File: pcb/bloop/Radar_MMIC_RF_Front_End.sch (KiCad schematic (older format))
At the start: 1 part

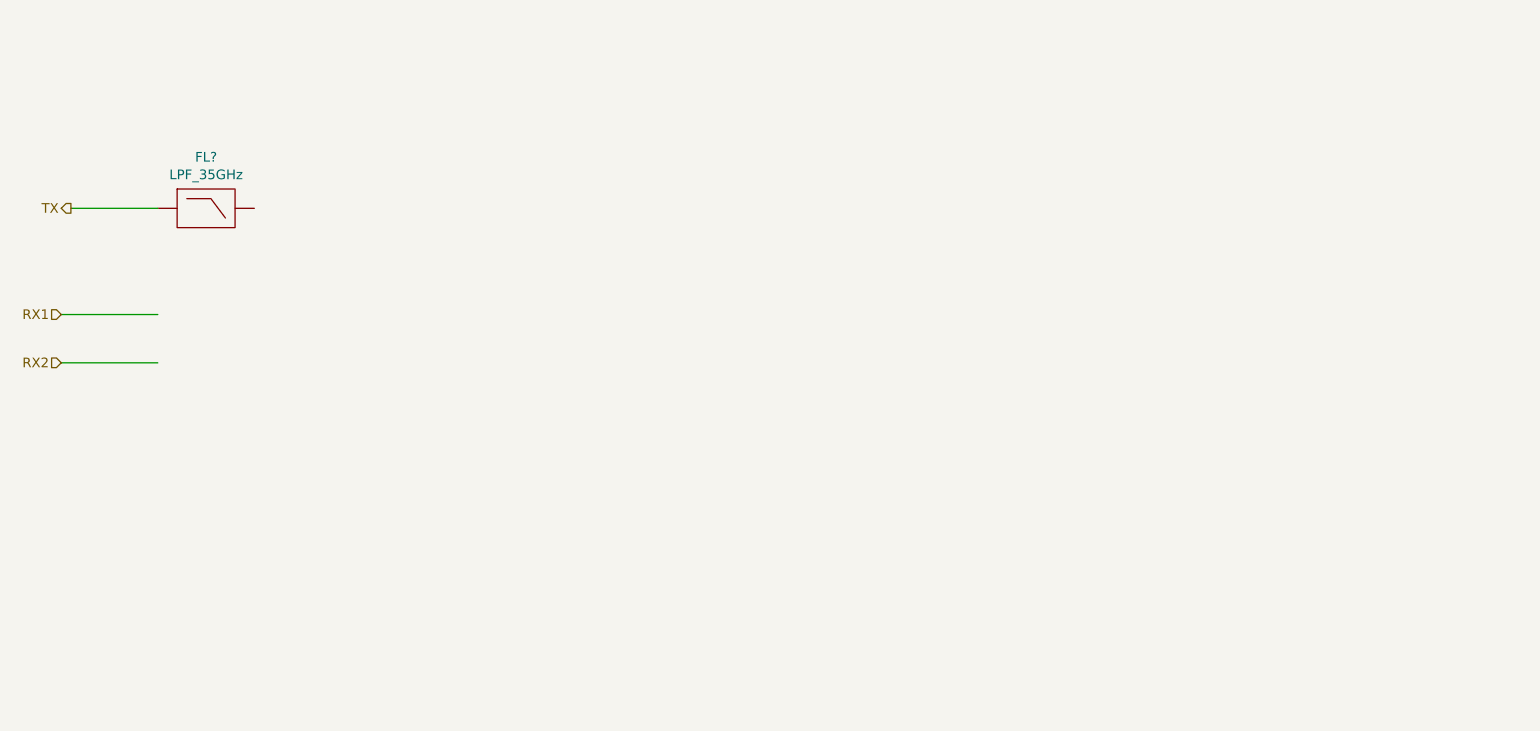
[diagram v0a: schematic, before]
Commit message: Added 3d SMP footprint and model
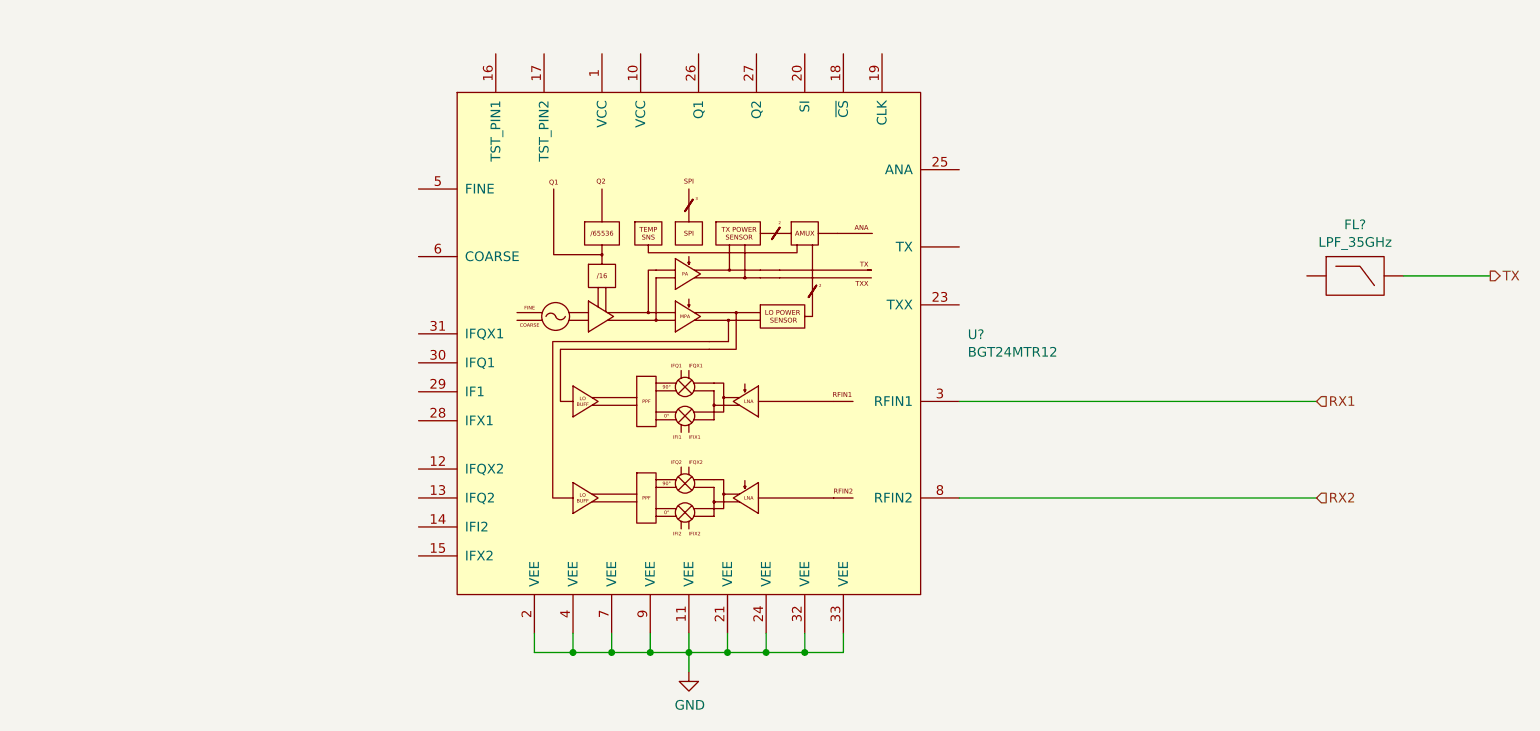
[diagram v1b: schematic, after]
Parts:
- added U?: BGT24MTR12, symbol bloop:BGT24MTR12
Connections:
- net labels added: GND
- wire segments 3 -> 21
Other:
- moved on the sheet: FL?
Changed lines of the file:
@@
 L bloop:LPF_35GHz FL?
 U 1 1 5D3D6E0E
-P 3200 2500
-F 0 "FL?" H 3200 2765 50  0000 C CNN
-F 1 "LPF_35GHz" H 3200 2674 50  0000 C CNN
-F 2 "bloop:35GHz_LPF" H 3200 2250 50  0001 C CNN
-F 3 "" H 2700 2750 50  0001 C CNN
-	1    3200 2500
+P 9150 2850
+F 0 "FL?" H 9150 3115 50  0000 C CNN
+F 1 "LPF_35GHz" H 9150 3024 50  0000 C CNN
+F 2 "bloop:35GHz_LPF" H 9150 2600 50  0001 C CNN
+F 3 "" H 8650 3100 50  0001 C CNN
+	1    9150 2850
 	1    0    0    -1
 $EndComp
 Wire Wire Line
-	2950 2500 2500 2500
-Text HLabel 2500 2500 0    50   Output ~ 0
+	9850 2850 9400 2850
+Text HLabel 9850 2850 2    50   Output ~ 0
 TX
-Text HLabel 2450 3050 0    50   Input ~ 0
+Text HLabel 8950 3500 2    50   Input ~ 0
 RX1
-Text HLabel 2450 3300 0    50   Input ~ 0
+Text HLabel 8950 4000 2    50   Input ~ 0
 RX2
+$Comp
+L bloop:BGT24MTR12 U?
+U 1 1 5D3E6B28
+P 5700 3200
+F 0 "U?" H 7144 3246 50  0000 L CNN
+F 1 "BGT24MTR12" H 7144 3155 50  0000 L CNN
+F 2 "" H 5700 5600 50  0001 C CNN
+F 3 "" H 5700 5600 50  0001 C CNN
+	1    5700 3200
+	1    0    0    -1
+$EndComp
 Wire Wire Line
-	2450 3050 2950 3050
+	4900 4700 4900 4800
 Wire Wire Line
-	2450 3300 2950 3300
+	4900 4800 5100 4800
+Wire Wire Line
+	6500 4800 6500 4700
+Wire Wire Line
+	6300 4700 6300 4800
+Connection ~ 6300 4800
+Wire Wire Line
+	6300 4800 6500 4800
+Wire Wire Line
+	6100 4700 6100 4800
+Connection ~ 6100 4800
+Wire Wire Line
+	6100 4800 6300 4800
+Wire Wire Line
+	5900 4700 5900 4800
+Connection ~ 5900 4800
+Wire Wire Line
+	5900 4800 6100 4800
+Wire Wire Line
+	5700 4700 5700 4800
+Connection ~ 5700 4800
+Wire Wire Line
+	5700 4800 5900 4800
+Wire Wire Line
+	5500 4700 5500 4800
+Connection ~ 5500 4800
+Wire Wire Line
+	5500 4800 5700 4800
+Wire Wire Line
+	5300 4700 5300 4800
+Connection ~ 5300 4800
+Wire Wire Line
+	5300 4800 5500 4800
+Wire Wire Line
+	5100 4700 5100 4800
+Connection ~ 5100 4800
+Wire Wire Line
+	5100 4800 5300 4800
+$Comp
+L power:GND #PWR?
+U 1 1 5D3EEAEA
+P 5700 4900
+F 0 "#PWR?" H 5700 4650 50  0001 C CNN
+F 1 "GND" H 5705 4727 50  0000 C CNN
+F 2 "" H 5700 4900 50  0001 C CNN
+F 3 "" H 5700 4900 50  0001 C CNN
+	1    5700 4900
+	1    0    0    -1
+$EndComp
+Wire Wire Line
+	5700 4900 5700 4800
+Wire Wire Line
+	8950 3500 7100 3500
+Wire Wire Line
+	7100 4000 8950 4000
 $EndSCHEMATC

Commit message: Added BGT24MTR12 VQFN-32-9 footprint Updated gold material on 3d model 734153320
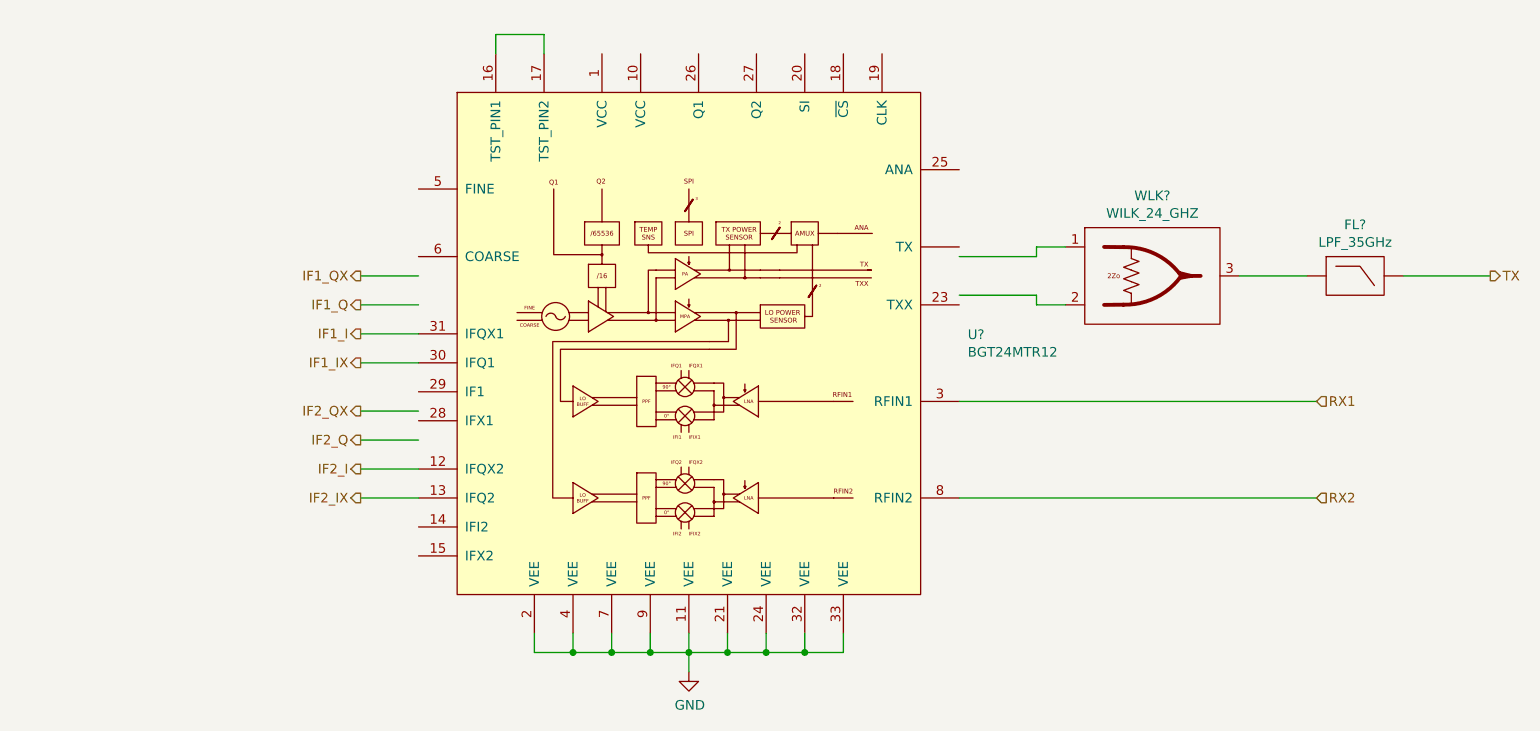
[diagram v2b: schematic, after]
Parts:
- added WLK?: WILK_24_GHZ, symbol bloop:WILK_24_GHZ
- U?: footprint (none) -> bloop:BGT24MTR12; MPN (none) -> BGT24MTR12E6327XUMA1
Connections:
- net labels added: IF1_I, IF1_IX, IF1_Q, IF1_QX, IF2_I, IF2_IX, IF2_Q, IF2_QX
- wire segments 21 -> 39
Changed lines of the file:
@@
 F 0 "U?" H 7144 3246 50  0000 L CNN
 F 1 "BGT24MTR12" H 7144 3155 50  0000 L CNN
-F 2 "" H 5700 5600 50  0001 C CNN
-F 3 "" H 5700 5600 50  0001 C CNN
+F 2 "bloop:BGT24MTR12" H 5700 5600 50  0001 C CNN
+F 3 "https://www.infineon.com/dgdl/Infineon-BGT24MTR12-DS-v03_01-EN.pdf?fileId=db3a304339dcf4b10139df108e75025b" H 5700 5600 50  0001 C CNN
+F 4 "BGT24MTR12E6327XUMA1" H 5700 3200 50  0001 C CNN "MPN"
 	1    5700 3200
 	1    0    0    -1
@@
 Wire Wire Line
 	7100 4000 8950 4000
+$Comp
+L bloop:WILK_24_GHZ WLK?
+U 1 1 5D3D6313
+P 8100 2850
+F 0 "WLK?" H 8100 3265 50  0000 C CNN
+F 1 "WILK_24_GHZ" H 8100 3174 50  0000 C CNN
+F 2 "" H 8100 3200 50  0001 C CNN
+F 3 "" H 8100 3200 50  0001 C CNN
+	1    8100 2850
+	1    0    0    -1
+$EndComp
+Wire Wire Line
+	7100 2750 7500 2750
+Wire Wire Line
+	7500 2750 7500 2700
+Wire Wire Line
+	7500 2700 7650 2700
+Wire Wire Line
+	7100 2950 7500 2950
+Wire Wire Line
+	7500 2950 7500 3000
+Wire Wire Line
+	7500 3000 7650 3000
+Wire Wire Line
+	8550 2850 8900 2850
+Wire Wire Line
+	4300 2850 4000 2850
+Wire Wire Line
+	4300 3000 4000 3000
+Wire Wire Line
+	4300 3150 4000 3150
+Wire Wire Line
+	4300 3300 4000 3300
+Wire Wire Line
+	4300 3550 4000 3550
+Wire Wire Line
+	4300 3700 4000 3700
+Wire Wire Line
+	4300 3850 4000 3850
+Wire Wire Line
+	4300 4000 4000 4000
+Text HLabel 4000 2850 0    50   Output ~ 0
+IF1_QX
+Text HLabel 4000 3000 0    50   Output ~ 0
+IF1_Q
+Text HLabel 4000 3150 0    50   Output ~ 0
+IF1_I
+Text HLabel 4000 3300 0    50   Output ~ 0
+IF1_IX
+Text HLabel 4000 3550 0    50   Output ~ 0
+IF2_QX
+Text HLabel 4000 3700 0    50   Output ~ 0
+IF2_Q
+Text HLabel 4000 3850 0    50   Output ~ 0
+IF2_I
+Text HLabel 4000 4000 0    50   Output ~ 0
+IF2_IX
+Wire Wire Line
+	4700 1700 4700 1600
+Wire Wire Line
+	4700 1600 4950 1600
+Wire Wire Line
+	4950 1600 4950 1700
 $EndSCHEMATC

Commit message: Rearrange pins for aesthetic reasons
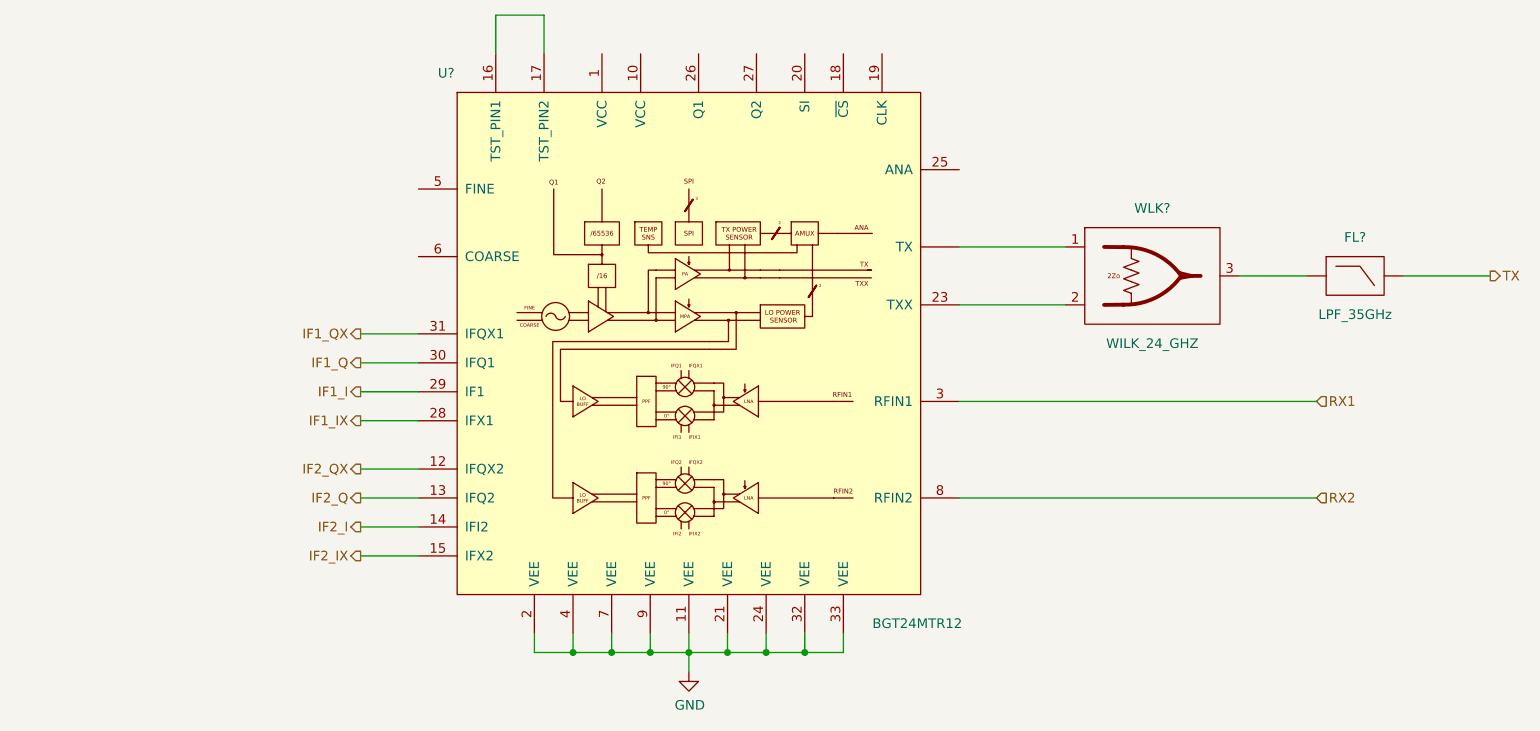
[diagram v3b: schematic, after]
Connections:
- wire segments 39 -> 35
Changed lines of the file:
@@
 U 1 1 5D3D6E0E
 P 9150 2850
-F 0 "FL?" H 9150 3115 50  0000 C CNN
-F 1 "LPF_35GHz" H 9150 3024 50  0000 C CNN
+F 0 "FL?" H 9150 3050 50  0000 C CNN
+F 1 "LPF_35GHz" H 9150 2650 50  0000 C CNN
 F 2 "bloop:35GHz_LPF" H 9150 2600 50  0001 C CNN
 F 3 "" H 8650 3100 50  0001 C CNN
@@
 U 1 1 5D3E6B28
 P 5700 3200
-F 0 "U?" H 7144 3246 50  0000 L CNN
-F 1 "BGT24MTR12" H 7144 3155 50  0000 L CNN
+F 0 "U?" H 4400 4600 50  0000 L CNN
+F 1 "BGT24MTR12" H 6650 1750 50  0000 L CNN
 F 2 "bloop:BGT24MTR12" H 5700 5600 50  0001 C CNN
 F 3 "https://www.infineon.com/dgdl/Infineon-BGT24MTR12-DS-v03_01-EN.pdf?fileId=db3a304339dcf4b10139df108e75025b" H 5700 5600 50  0001 C CNN
@@
 U 1 1 5D3D6313
 P 8100 2850
-F 0 "WLK?" H 8100 3265 50  0000 C CNN
-F 1 "WILK_24_GHZ" H 8100 3174 50  0000 C CNN
+F 0 "WLK?" H 8100 3200 50  0000 C CNN
+F 1 "WILK_24_GHZ" H 8100 2500 50  0000 C CNN
 F 2 "" H 8100 3200 50  0001 C CNN
 F 3 "" H 8100 3200 50  0001 C CNN
@@
 $EndComp
 Wire Wire Line
-	7100 2750 7500 2750
+	7100 2700 7650 2700
 Wire Wire Line
-	7500 2750 7500 2700
-Wire Wire Line
-	7500 2700 7650 2700
-Wire Wire Line
-	7100 2950 7500 2950
-Wire Wire Line
-	7500 2950 7500 3000
-Wire Wire Line
-	7500 3000 7650 3000
+	7100 3000 7650 3000
 Wire Wire Line
 	8550 2850 8900 2850
-Wire Wire Line
-	4300 2850 4000 2850
-Wire Wire Line
-	4300 3000 4000 3000
 Wire Wire Line
 	4300 3150 4000 3150
@@
 	4300 3300 4000 3300
 Wire Wire Line
-	4300 3550 4000 3550
+	4300 3450 4000 3450
 Wire Wire Line
-	4300 3700 4000 3700
+	4300 3600 4000 3600
 Wire Wire Line
 	4300 3850 4000 3850
 Wire Wire Line
 	4300 4000 4000 4000
-Text HLabel 4000 2850 0    50   Output ~ 0
+Wire Wire Line
+	4300 4150 4000 4150
+Wire Wire Line
+	4300 4300 4000 4300
+Text HLabel 4000 3150 0    50   Output ~ 0
 IF1_QX
-Text HLabel 4000 3000 0    50   Output ~ 0
+Text HLabel 4000 3300 0    50   Output ~ 0
 IF1_Q
-Text HLabel 4000 3150 0    50   Output ~ 0
+Text HLabel 4000 3450 0    50   Output ~ 0
 IF1_I
-Text HLabel 4000 3300 0    50   Output ~ 0
+Text HLabel 4000 3600 0    50   Output ~ 0
 IF1_IX
-Text HLabel 4000 3550 0    50   Output ~ 0
+Text HLabel 4000 3850 0    50   Output ~ 0
 IF2_QX
-Text HLabel 4000 3700 0    50   Output ~ 0
+Text HLabel 4000 4000 0    50   Output ~ 0
 IF2_Q
-Text HLabel 4000 3850 0    50   Output ~ 0
+Text HLabel 4000 4150 0    50   Output ~ 0
 IF2_I
-Text HLabel 4000 4000 0    50   Output ~ 0
+Text HLabel 4000 4300 0    50   Output ~ 0
 IF2_IX
 Wire Wire Line
-	4700 1700 4700 1600
+	4700 1700 4700 1500
 Wire Wire Line
-	4700 1600 4950 1600
+	4700 1500 4950 1500
 Wire Wire Line
-	4950 1600 4950 1700
+	4950 1500 4950 1700
 $EndSCHEMATC
